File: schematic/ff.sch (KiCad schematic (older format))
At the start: 7 parts, among them IC1 ATTINY13A-P

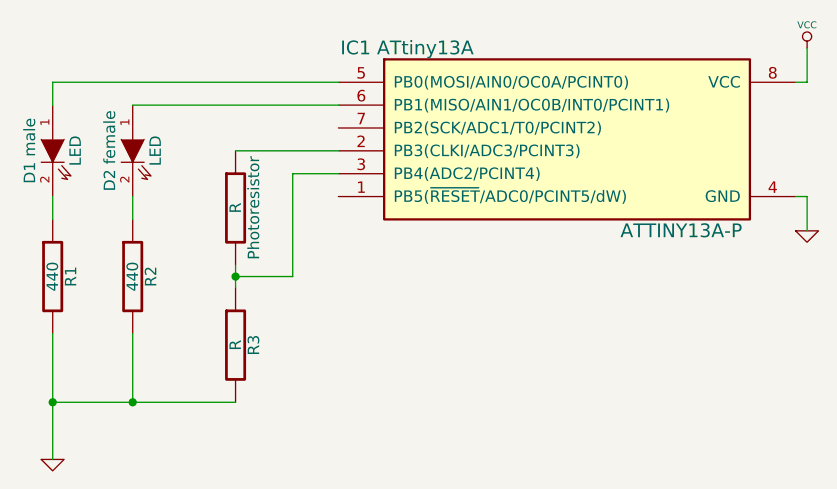
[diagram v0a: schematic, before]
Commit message: schematic picture tweaks
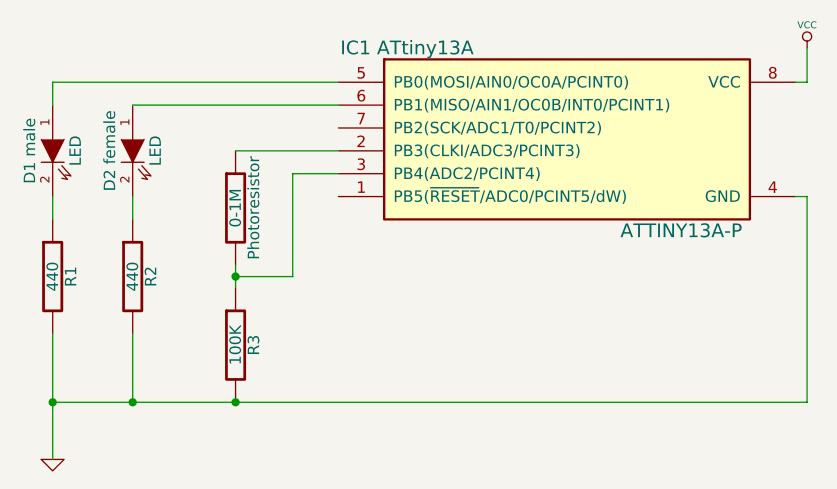
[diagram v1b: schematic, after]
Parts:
- Photoresistor: value R -> 0-1M
- R3: value R -> 100K
- renumbered D1 to D1~male, D2 to D2~female, IC1 to IC1~ATtiny13A
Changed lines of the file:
@@
-EESchema Schematic File Version 2  date Tue 17 Sep 2013 01:51:18 AM PDT
+EESchema Schematic File Version 2  date Tue 17 Sep 2013 07:05:57 AM PDT
 LIBS:power
 LIBS:device
@@
 $EndDescr
 Wire Wire Line
-	4100 3650 4350 3650
+	3300 4200 6600 4200
 Wire Wire Line
-	4350 3650 4350 3200
+	6600 4200 6600 3300
 Wire Wire Line
-	4350 3200 4550 3200
+	6600 3300 6550 3300
 Wire Wire Line
-	4100 4200 3300 4200
+	4100 3100 4550 3100
+Connection ~ 3650 4200
+Wire Wire Line
+	3300 3900 3300 4450
+Wire Wire Line
+	3300 3300 3300 3400
+Wire Wire Line
+	4550 2900 3650 2900
+Wire Wire Line
+	6600 2650 6600 2800
+Wire Wire Line
+	6600 2800 6550 2800
+Wire Wire Line
+	4550 2800 3300 2800
+Wire Wire Line
+	3300 2800 3300 2900
+Wire Wire Line
+	3650 3300 3650 3400
+Connection ~ 4100 3650
+Connection ~ 3300 4200
+Wire Wire Line
+	4100 3700 4100 3600
 Wire Wire Line
 	3650 4200 3650 3900
 Wire Wire Line
-	4100 3700 4100 3600
-Connection ~ 3300 4200
-Connection ~ 4100 3650
+	4550 3200 4350 3200
 Wire Wire Line
-	3650 3300 3650 3400
+	4350 3200 4350 3650
 Wire Wire Line
-	3300 2900 3300 2800
-Wire Wire Line
-	3300 2800 4550 2800
-Wire Wire Line
-	6600 3450 6600 3300
-Wire Wire Line
-	6600 3300 6550 3300
-Wire Wire Line
-	6550 2800 6600 2800
-Wire Wire Line
-	6600 2800 6600 2650
-Wire Wire Line
-	4550 2900 3650 2900
-Wire Wire Line
-	3300 3300 3300 3400
-Wire Wire Line
-	3300 3900 3300 4450
-Connection ~ 3650 4200
-Wire Wire Line
-	4100 3100 4550 3100
+	4350 3650 4100 3650
+Connection ~ 4100 4200
 $Comp
 L R R3
@@
 P 4100 3950
 F 0 "R3" V 4180 3950 50  0000 C CNN
-F 1 "R" V 4100 3950 50  0000 C CNN
+F 1 "100K" V 4100 3950 50  0000 C CNN
 	1    4100 3950
 	1    0    0    -1
@@
 P 4100 3350
 F 0 "Photoresistor" V 4180 3350 50  0000 C CNN
-F 1 "R" V 4100 3350 50  0000 C CNN
+F 1 "0-1M" V 4100 3350 50  0000 C CNN
 	1    4100 3350
 	1    0    0    -1
@@
 F 1 "GND" H 3300 4380 30  0001 C CNN
 	1    3300 4450
-	1    0    0    -1
-$EndComp
-$Comp
-L GND #PWR?
-U 1 1 52380A43
-P 6600 3450
-F 0 "#PWR?" H 6600 3450 30  0001 C CNN
-F 1 "GND" H 6600 3380 30  0001 C CNN
-	1    6600 3450
 	1    0    0    -1
 $EndComp
@@
 $EndComp
 $Comp
-L LED D2
+L LED D2~female
 U 1 1 5238092C
 P 3650 3100
@@
 $EndComp
 $Comp
-L LED D1
+L LED D1~male
 U 1 1 523804D6
 P 3300 3100
@@
 $EndComp
 $Comp
-L ATTINY13A-P IC1
+L ATTINY13A-P IC1~ATtiny13A
 U 1 1 52380490
 P 4750 2700

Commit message: adjusted value of R3
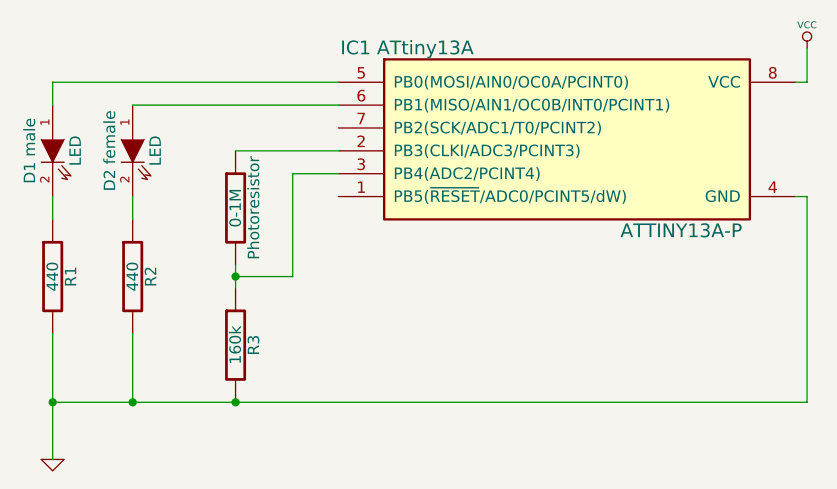
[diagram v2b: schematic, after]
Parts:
- R3: value 100K -> 160k
- renumbered D2~female to D2
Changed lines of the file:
@@
-EESchema Schematic File Version 2  date Tue 17 Sep 2013 07:05:57 AM PDT
+EESchema Schematic File Version 2  date Wed 25 Sep 2013 09:21:01 PM PDT
 LIBS:power
 LIBS:device
@@
 Sheet 1 1
 Title "Firefly"
-Date "17 sep 2013"
+Date "26 sep 2013"
 Rev ""
 Comp ""
@@
 $EndDescr
 Wire Wire Line
-	3300 4200 6600 4200
+	3300 4200 3650 4200
+Wire Wire Line
+	3650 4200 4100 4200
+Wire Wire Line
+	4100 4200 6600 4200
 Wire Wire Line
 	6600 4200 6600 3300
@@
 Connection ~ 3650 4200
 Wire Wire Line
-	3300 3900 3300 4450
+	3300 3900 3300 4200
+Wire Wire Line
+	3300 4200 3300 4450
 Wire Wire Line
 	3300 3300 3300 3400
@@
 Connection ~ 3300 4200
 Wire Wire Line
-	4100 3700 4100 3600
+	4100 3700 4100 3650
+Wire Wire Line
+	4100 3650 4100 3600
 Wire Wire Line
 	3650 4200 3650 3900
@@
 P 4100 3950
 F 0 "R3" V 4180 3950 50  0000 C CNN
-F 1 "100K" V 4100 3950 50  0000 C CNN
+F 1 "160k" V 4100 3950 50  0000 C CNN
 	1    4100 3950
 	1    0    0    -1
@@
 $EndComp
 $Comp
-L LED D2~female
+L LED D2
 U 1 1 5238092C
 P 3650 3100

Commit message: removed a resistor; both LEDs may use the same resistor, as they never light at the same time
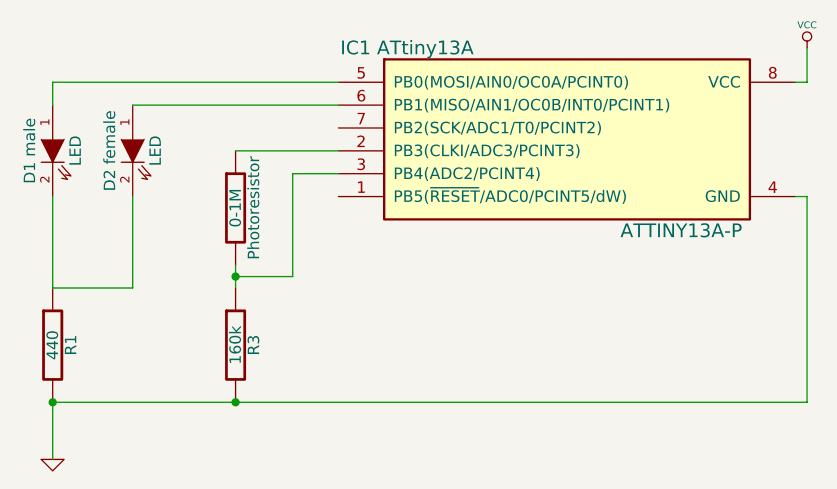
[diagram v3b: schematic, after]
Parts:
- removed R2: 440, symbol R
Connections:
- net at D1~male.2 (K), R1.1: now also D2.2 (K)
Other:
- moved on the sheet: R1
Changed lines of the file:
@@
-EESchema Schematic File Version 2  date Wed 25 Sep 2013 09:21:01 PM PDT
+EESchema Schematic File Version 2  date Sun 29 Sep 2013 01:58:59 PM PDT
 LIBS:power
 LIBS:device
@@
 Sheet 1 1
 Title "Firefly"
-Date "26 sep 2013"
+Date "29 sep 2013"
 Rev ""
 Comp ""
@@
 $EndDescr
 Wire Wire Line
-	3300 4200 3650 4200
+	3300 4450 3300 4200
 Wire Wire Line
-	3650 4200 4100 4200
+	3300 3300 3300 3700
+Connection ~ 4100 4200
 Wire Wire Line
-	4100 4200 6600 4200
+	4100 3650 4350 3650
 Wire Wire Line
-	6600 4200 6600 3300
+	4350 3650 4350 3200
 Wire Wire Line
-	6600 3300 6550 3300
+	4350 3200 4550 3200
 Wire Wire Line
-	4100 3100 4550 3100
-Connection ~ 3650 4200
+	4100 3600 4100 3700
+Connection ~ 3300 4200
+Connection ~ 4100 3650
 Wire Wire Line
-	3300 3900 3300 4200
+	3300 2900 3300 2800
 Wire Wire Line
-	3300 4200 3300 4450
+	3300 2800 4550 2800
 Wire Wire Line
-	3300 3300 3300 3400
+	6550 2800 6600 2800
+Wire Wire Line
+	6600 2800 6600 2650
 Wire Wire Line
 	4550 2900 3650 2900
 Wire Wire Line
-	6600 2650 6600 2800
+	4100 3100 4550 3100
 Wire Wire Line
-	6600 2800 6550 2800
+	6550 3300 6600 3300
 Wire Wire Line
-	4550 2800 3300 2800
+	6600 3300 6600 4200
 Wire Wire Line
-	3300 2800 3300 2900
+	3650 3300 3650 3700
 Wire Wire Line
-	3650 3300 3650 3400
-Connection ~ 4100 3650
-Connection ~ 3300 4200
+	3650 3700 3300 3700
 Wire Wire Line
-	4100 3700 4100 3650
-Wire Wire Line
-	4100 3650 4100 3600
-Wire Wire Line
-	3650 4200 3650 3900
-Wire Wire Line
-	4550 3200 4350 3200
-Wire Wire Line
-	4350 3200 4350 3650
-Wire Wire Line
-	4350 3650 4100 3650
-Connection ~ 4100 4200
+	6600 4200 3300 4200
 $Comp
 L R R3
@@
 $EndComp
 $Comp
-L R R2
-U 1 1 52380938
-P 3650 3650
-F 0 "R2" V 3730 3650 50  0000 C CNN
-F 1 "440" V 3650 3650 50  0000 C CNN
-	1    3650 3650
-	1    0    0    -1
-$EndComp
-$Comp
 L LED D2
 U 1 1 5238092C
@@
 L R R1
 U 1 1 5238084E
-P 3300 3650
-F 0 "R1" V 3380 3650 50  0000 C CNN
-F 1 "440" V 3300 3650 50  0000 C CNN
-	1    3300 3650
+P 3300 3950
+F 0 "R1" V 3380 3950 50  0000 C CNN
+F 1 "440" V 3300 3950 50  0000 C CNN
+	1    3300 3950
 	1    0    0    -1
 $EndComp

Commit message: R1 is 350 ohm
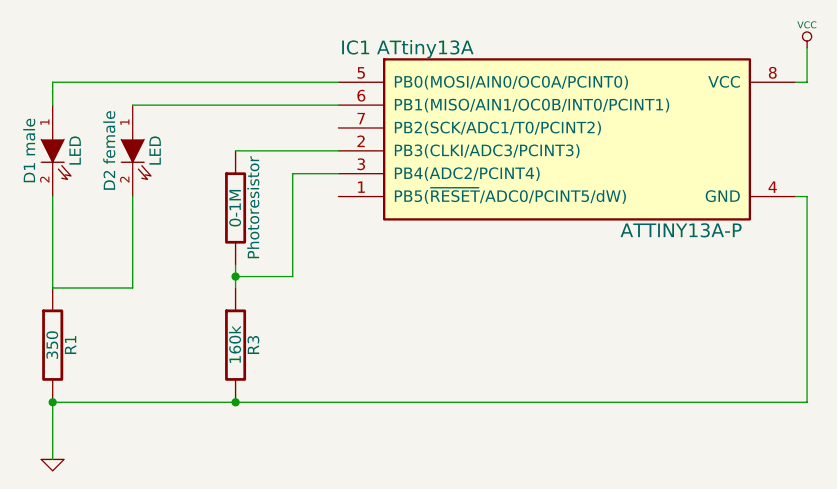
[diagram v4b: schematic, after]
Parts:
- R1: value 440 -> 350
- renumbered D2 to D2~female
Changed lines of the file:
@@
-EESchema Schematic File Version 2  date Sun 29 Sep 2013 01:58:59 PM PDT
+EESchema Schematic File Version 2  date Sun 29 Sep 2013 10:29:41 PM PDT
 LIBS:power
 LIBS:device
@@
 Sheet 1 1
 Title "Firefly"
-Date "29 sep 2013"
+Date "30 sep 2013"
 Rev ""
 Comp ""
@@
 $EndComp
 $Comp
-L LED D2
+L LED D2~female
 U 1 1 5238092C
 P 3650 3100
@@
 P 3300 3950
 F 0 "R1" V 3380 3950 50  0000 C CNN
-F 1 "440" V 3300 3950 50  0000 C CNN
+F 1 "350" V 3300 3950 50  0000 C CNN
 	1    3300 3950
 	1    0    0    -1
